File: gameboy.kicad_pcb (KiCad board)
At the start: 4 copper layers, 90 x 120 mm, 126 parts, among them J1 SM03B-SRSS-TB, J2 FPC-05F-40PH20, J3 Conn_01x02, J4 Conn_01x02, J5 Conn_01x02, J6 SD_Card_Receptacle, J7 USB_C_Receptacle_USB2.0_16P, Q2 AO3401A, Q3 SS8050, Q5 SS8050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

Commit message: changes after testing the display
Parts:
- removed R11, R9: 10R, Resistor_SMD:R_0603_1608Metric
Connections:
- J2 pad 35: Net-(J2-Pin_35) -> Net-(J2-Pin_34)
- J2 pad 36: Net-(J2-Pin_36) -> Net-(J2-Pin_34)
- R10 pad 1: Net-(J2-Pin_35) -> Net-(J2-Pin_34)
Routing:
- net Net-(Q5-C): track 6.27 -> 1.67 mm
- net Net-(J2-Pin_36): track 2.78 -> 0.00 mm
- net Net-(J2-Pin_35): track 2.55 -> 0.00 mm
- net Net-(J2-Pin_34): track 2.85 -> 3.43 mm

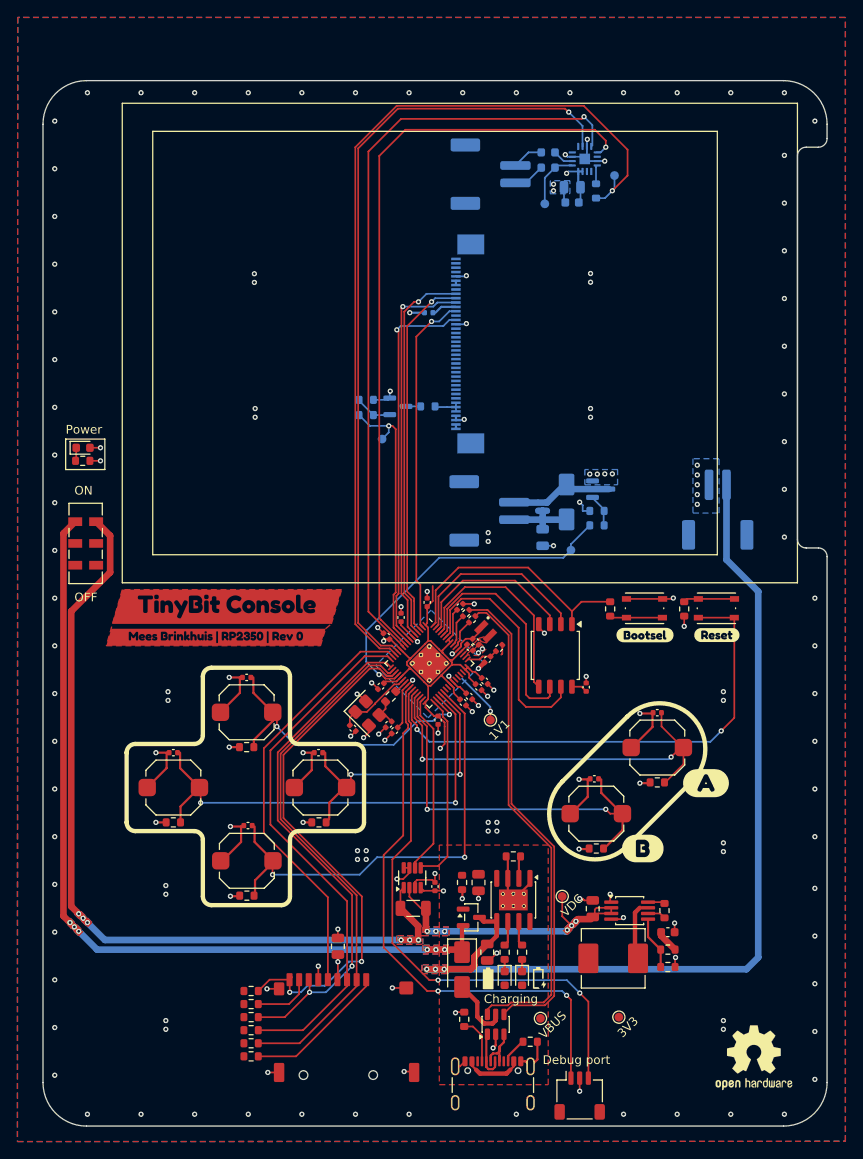
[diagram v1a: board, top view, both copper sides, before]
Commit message: add fiducials and mounting holes
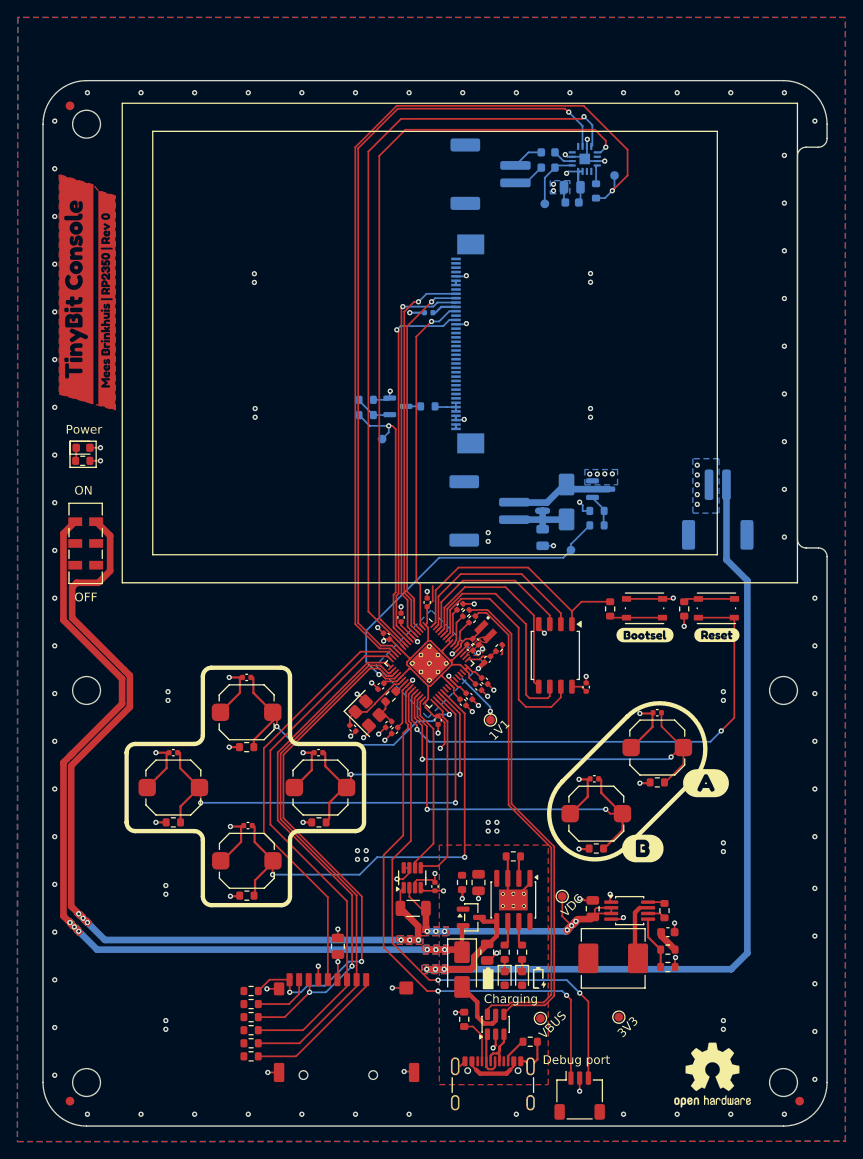
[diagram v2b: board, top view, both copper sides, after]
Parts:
- added REF**: Fiducial_1mm_Mask2mm, Fiducial:Fiducial_1mm_Mask2mm, F.Cu at (102.0, 148.5)
- added REF**: MountingHole_3.2mm_M3, MountingHole:MountingHole_3.2mm_M3, F.Cu at (183.9, 146.4)
- added REF**: MountingHole_3.2mm_M3, MountingHole:MountingHole_3.2mm_M3, F.Cu at (183.9, 101.4)
- added REF**: MountingHole_3.2mm_M3, MountingHole:MountingHole_3.2mm_M3, F.Cu at (103.9, 146.4)
- added REF**: MountingHole_3.2mm_M3, MountingHole:MountingHole_3.2mm_M3, F.Cu at (103.9, 36.4)
- added REF**: MountingHole_3.2mm_M3, MountingHole:MountingHole_3.2mm_M3, F.Cu at (103.9, 101.4)
- added REF**: Fiducial_1mm_Mask2mm, Fiducial:Fiducial_1mm_Mask2mm, F.Cu at (185.8, 148.5)
- added REF**: Fiducial_1mm_Mask2mm, Fiducial:Fiducial_1mm_Mask2mm, F.Cu at (102.0, 34.2)
- moved kibuzzard-69734872 40.6 mm to (106.2, 56.6), turned to 90 degrees
- moved kibuzzard-697346E9 40.3 mm to (102.7, 55.3), turned to 90 degrees
- moved REF** 5.15 mm to (175.8, 145.5)
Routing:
- net Net-(U4-IN+): track 99.0 -> 105.9 mm
- net Net-(D3-K): track 103.4 -> 109.4 mm
- net /Power/BAT+: track 110.4 -> 108.4 mm

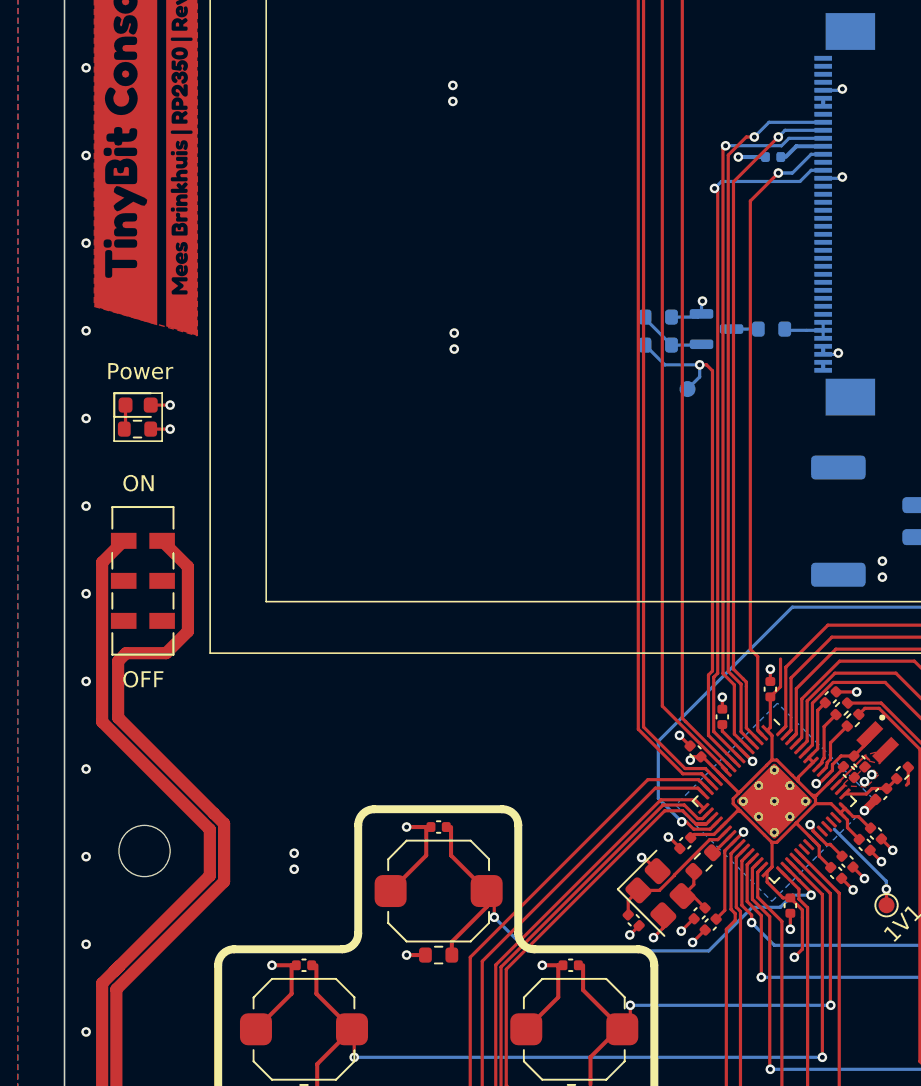
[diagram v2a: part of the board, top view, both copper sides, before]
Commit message: move capacitor lcd
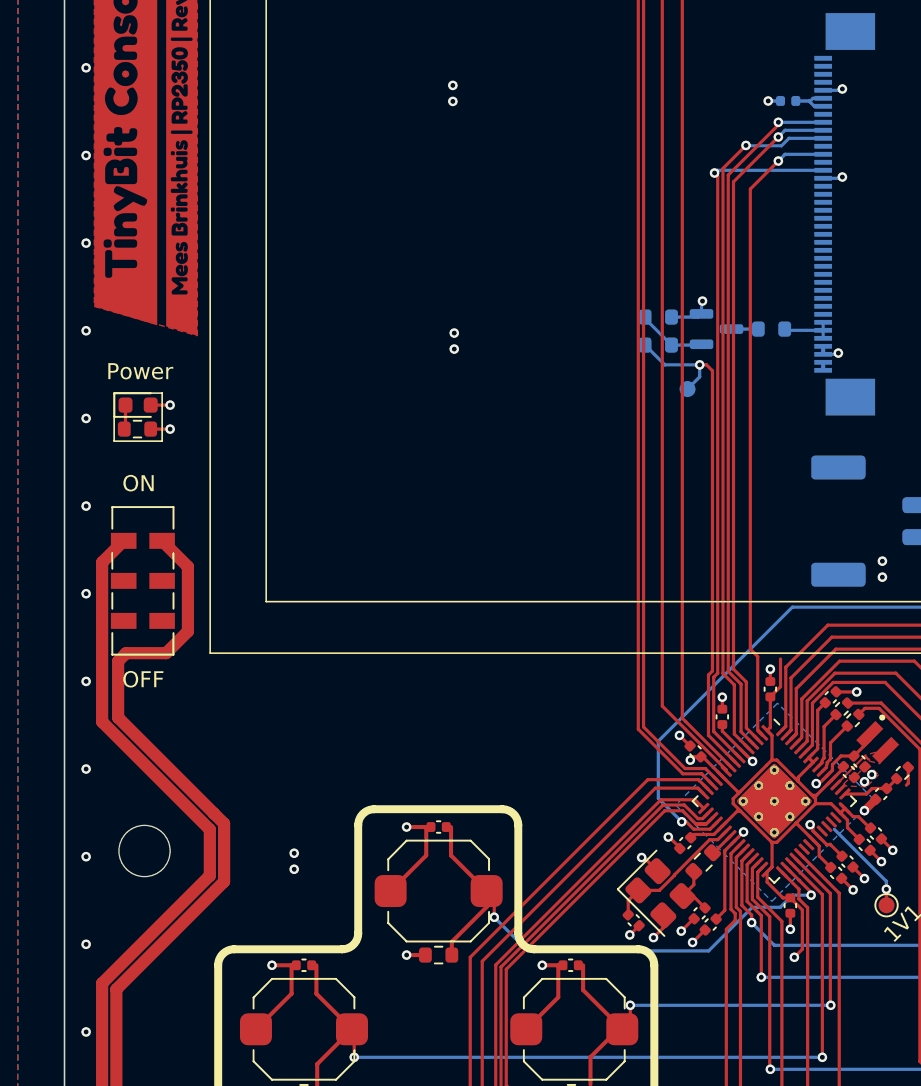
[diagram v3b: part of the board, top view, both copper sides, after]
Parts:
- moved C17 3.62 mm to (144.1, 54.5)
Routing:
- net +3V3: track 98.4 -> 97.6 mm
- net /LCD/LCD_DC: track 44.7 -> 44.0 mm
- net /LCD/LCD_CS: track 44.2 -> 43.6 mm
- net GND: track 123.8 -> 123.2 mm
- net /LCD/LCD_RST: track 43.7 -> 44.3 mm

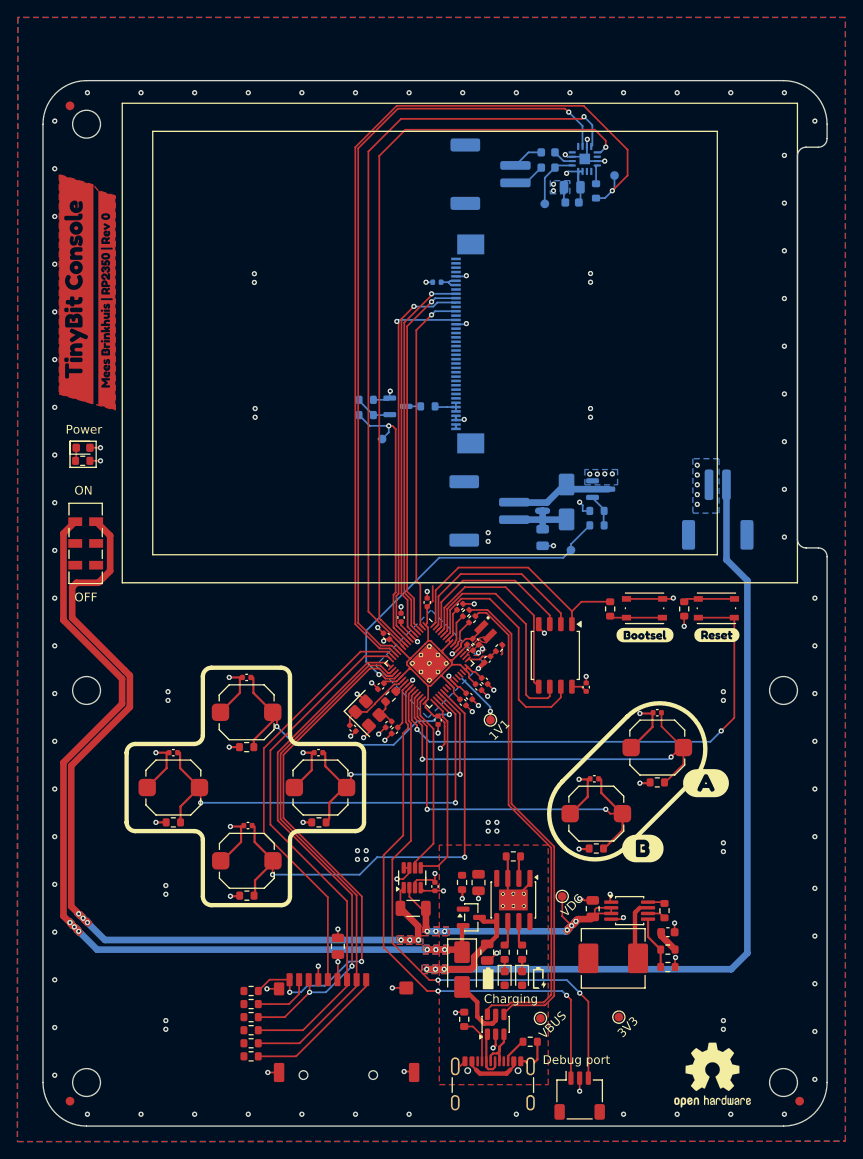
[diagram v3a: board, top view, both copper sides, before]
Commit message: battery polarity and position
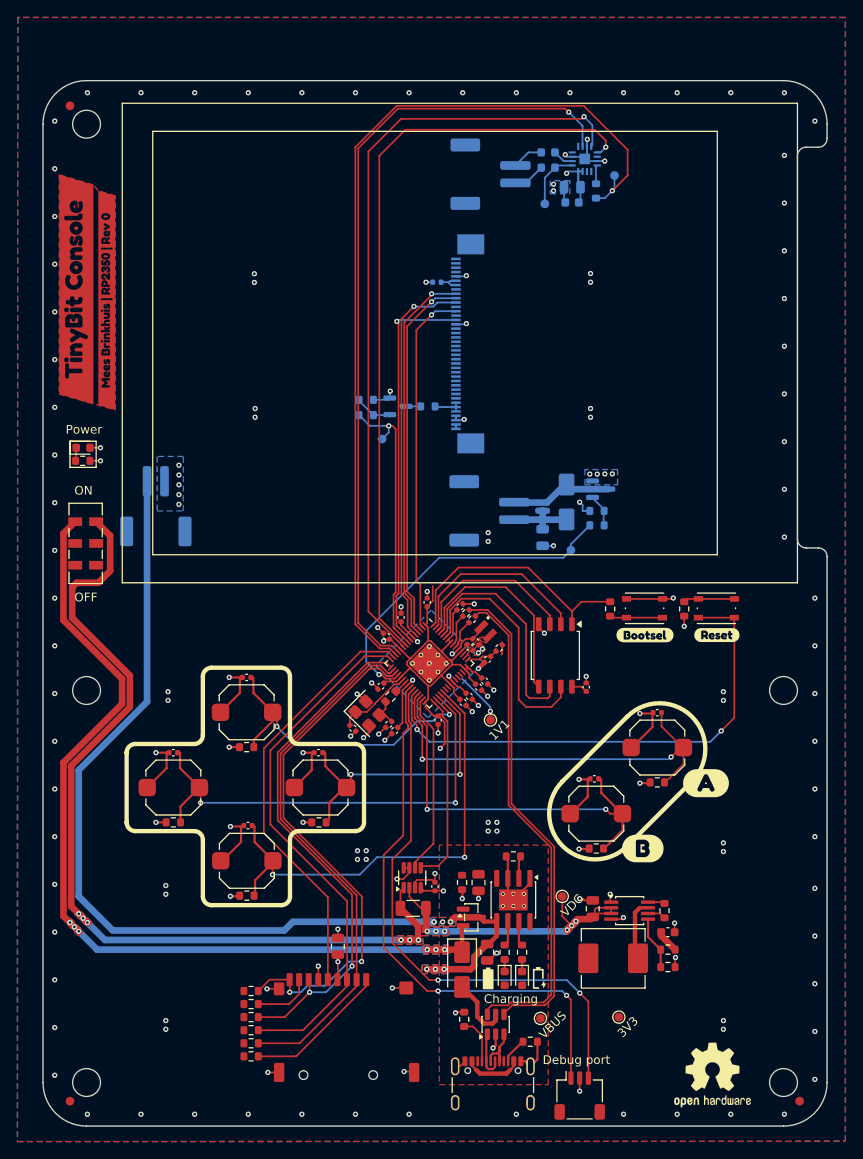
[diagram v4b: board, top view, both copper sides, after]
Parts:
- moved J3 64.5 mm to (111.8, 80.2)
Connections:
- C24 pad 1: /Power/BAT+ -> /Power/BAT-
- J3 pad 1: /Power/BAT+ -> GND
- J3 pad 2: GND -> /Power/BAT-
- Q2 pad 3: /Power/BAT+ -> /Power/BAT-
- U3 pad 5: /Power/BAT+ -> /Power/BAT-
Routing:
- net /Power/BAT-: track 0.00 -> 113.3 mm, vias 0 -> 4
- net /Power/BAT+: track 108.4 -> 0.00 mm, vias 3 -> 0
- net /Power/USB_VBUS: vias 0 -> 2
- added copper zone on B.Cu, net /Power/USB_VBUS
- removed copper zone on B.Cu, net /Power/BAT+
- removed copper zone on F.Cu, net /Power/BAT+
